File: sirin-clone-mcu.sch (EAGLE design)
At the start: 55 parts, among them J1 PJ-002A, J3 30_PIN_CONNECTOR_MALE, J5 SWITCHCRAFT_PHONEJACK, J6 SWD_CONNECTOR, T2 MCP1825S, U4 SGTL5000_32QFN, U5 23LC1024

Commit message: ready for gerbers
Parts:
- removed C4: 2.2UF, moon-germs-v1_main:2.2UF
- removed FUSE2: (no value), moon-germs-v1_main:FUSE
- removed U$2: USB-B, sirin-clone-library:USB-B
- added C2, C5: 1UF, sirin-clone-library:1UF
- added J2: (no value), sirin-clone-library:USB_MICRO-B_HALF_PTH_MILL
- L3: value FERRITE600 -> FER600
- R1: value 220OHM -> 220
- R2: value 470OHM -> 470
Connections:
- removed net N$27: J3.P$2
- removed net N$4: OK1.VO, R2.1
- removed net VUSB: FUSE2.2, U$2.VCC
- new net N$16: C5.-, U$3.6
- new net N$5: C5.+, U4.LINEOUTL(12)
- new net N$6: C2.+, U4.LINEOUTR(11)
- new net N$7: C2.-, U$3.5
- net AGND: now also J3.P$29, J3.P$30
- net D+: now also J2.D+; no longer U$2.D+
- net D-: now also J2.D-; no longer U$2.D-
- net GND: now also J2.GND, J2.SHIELD, J3.P$13, U$3.4; no longer C4.-, J3.P$29, J3.P$30, U$2.GND
- net PIN0/MIDIIN: now also OK1.VO, R2.1
- net PIN20/KNOB4: now also J3.P$3; no longer J3.P$4
- net PIN21/KNOB5: now also J3.P$4; no longer J3.P$5
- net PIN26/KNOB6: now also J3.P$8; no longer J3.P$9
- net PIN31/KNOB11: now also J3.P$7; no longer J3.P$8
- net PIN5/SW4: now also J3.P$5; no longer J3.P$6
- net PIN8/MIDILED: now also J3.P$2; no longer J3.P$3
- net PINA10/KNOB12: now also J3.P$10; no longer J3.P$11
- net PINA11/KNOB13: now also J3.P$9; no longer J3.P$10
- net PINA12/KNOB14: now also J3.P$11; no longer J3.P$12
- net PINA13/KNOB15: now also J3.P$12; no longer J3.P$13
- net PINA14/KNOB16: now also J3.P$6; no longer J3.P$7
- net USB_ID: now also J2.ID
- net VUSB_IN: now also J2.VBUS; no longer C4.+, FUSE2.1
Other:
- moved on the sheet: U$3

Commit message: adding bom attributes
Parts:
- J2: device sirin-clone-library:USB_MICRO-B_HALF_PTH_MILL -> sirin-clone-library:USB_MICRO-B
- L3: device moon-germs-v1_main:FERRITE600 -> moon-germs-v1_main:FERRITE600_AUDIO
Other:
- moved on the sheet: J2
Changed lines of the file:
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@@
 <part name="GND1" library="sirin-clone-library" library_urn="urn:adsk.eagle:library:9336050" deviceset="GND" device=""/>
 <part name="GND2" library="sirin-clone-library" library_urn="urn:adsk.eagle:library:9336050" deviceset="GND" device=""/>
-<part name="J3" library="sirin-clone-library" library_urn="urn:adsk.eagle:library:9336050" deviceset="30_PIN_CONNECTOR_MALE" device="" package3d_urn="urn:adsk.eagle:package:9975532/3"/>
+<part name="J3" library="sirin-clone-library" library_urn="urn:adsk.eagle:library:9336050" deviceset="30_PIN_CONNECTOR_MALE" device="" package3d_urn="urn:adsk.eagle:package:9975532/4"/>
 <part name="GND3" library="sirin-clone-library" library_urn="urn:adsk.eagle:library:9336050" deviceset="GND" device=""/>
 <part name="K3" library="moon-germs-v1_main" library_urn="urn:adsk.eagle:library:8442267" deviceset="MK20DX256VLH7" device="" package3d_urn="urn:adsk.eagle:package:8700970/2"/>
@@
 <part name="R5" library="moon-germs-v1_main" library_urn="urn:adsk.eagle:library:8442267" deviceset="33OHM" device="" package3d_urn="urn:adsk.eagle:package:8442354/2" value="33"/>
 <part name="R6" library="moon-germs-v1_main" library_urn="urn:adsk.eagle:library:8442267" deviceset="33OHM" device="" package3d_urn="urn:adsk.eagle:package:8442354/2" value="33"/>
-<part name="J6" library="moon-germs-v1_main" library_urn="urn:adsk.eagle:library:8442267" deviceset="SWD_CONNECTOR" device=""/>
+<part name="J6" library="moon-germs-v1_main" library_urn="urn:adsk.eagle:library:8442267" deviceset="SWD_CONNECTOR" device="" package3d_urn="urn:adsk.eagle:package:8709581/1"/>
 <part name="GND9" library="moon-germs-v1_main" library_urn="urn:adsk.eagle:library:8442267" deviceset="GND" device=""/>
 <part name="S2" library="moon-germs-v1_main" library_urn="urn:adsk.eagle:library:8442267" deviceset="TACT_SWITCH" device="" package3d_urn="urn:adsk.eagle:package:8762249/2"/>
@@
 <part name="C36" library="moon-germs-v1_main" library_urn="urn:adsk.eagle:library:8442267" deviceset="0.15UF" device="" package3d_urn="urn:adsk.eagle:package:8442351/2"/>
 <part name="D6" library="moon-germs-v1" deviceset="AP7313" device=""/>
-<part name="L3" library="moon-germs-v1_main" library_urn="urn:adsk.eagle:library:8442267" deviceset="FERRITE600" device="" package3d_urn="urn:adsk.eagle:package:8442354/2" value="FER600"/>
+<part name="L3" library="moon-germs-v1_main" library_urn="urn:adsk.eagle:library:8442267" deviceset="FERRITE600_AUDIO" device="" package3d_urn="urn:adsk.eagle:package:8442354/2" value="FER600"/>
 <part name="R11" library="moon-germs-v1_main" library_urn="urn:adsk.eagle:library:8442267" deviceset="2.2KOHM" device="" package3d_urn="urn:adsk.eagle:package:8442354/2" value="2.2K"/>
 <part name="R12" library="moon-germs-v1_main" library_urn="urn:adsk.eagle:library:8442267" deviceset="2.2KOHM" device="" package3d_urn="urn:adsk.eagle:package:8442354/2" value="2.2K"/>
@@
 <part name="C5" library="sirin-clone-library" library_urn="urn:adsk.eagle:library:9336050" deviceset="1UF" device="" package3d_urn="urn:adsk.eagle:package:8442351/2"/>
 <part name="GND20" library="sirin-clone-library" library_urn="urn:adsk.eagle:library:9336050" deviceset="GND" device=""/>
-<part name="J2" library="sirin-clone-library" library_urn="urn:adsk.eagle:library:9336050" deviceset="USB_MICRO-B" device="_HALF_PTH_MILL" package3d_urn="urn:adsk.eagle:package:8711132/2"/>
+<part name="J2" library="sirin-clone-library" library_urn="urn:adsk.eagle:library:9336050" deviceset="USB_MICRO-B" device="" package3d_urn="urn:adsk.eagle:package:10018607/2"/>
 <part name="GND8" library="moon-germs-v1_main" library_urn="urn:adsk.eagle:library:8442267" deviceset="GND" device=""/>
 </parts>

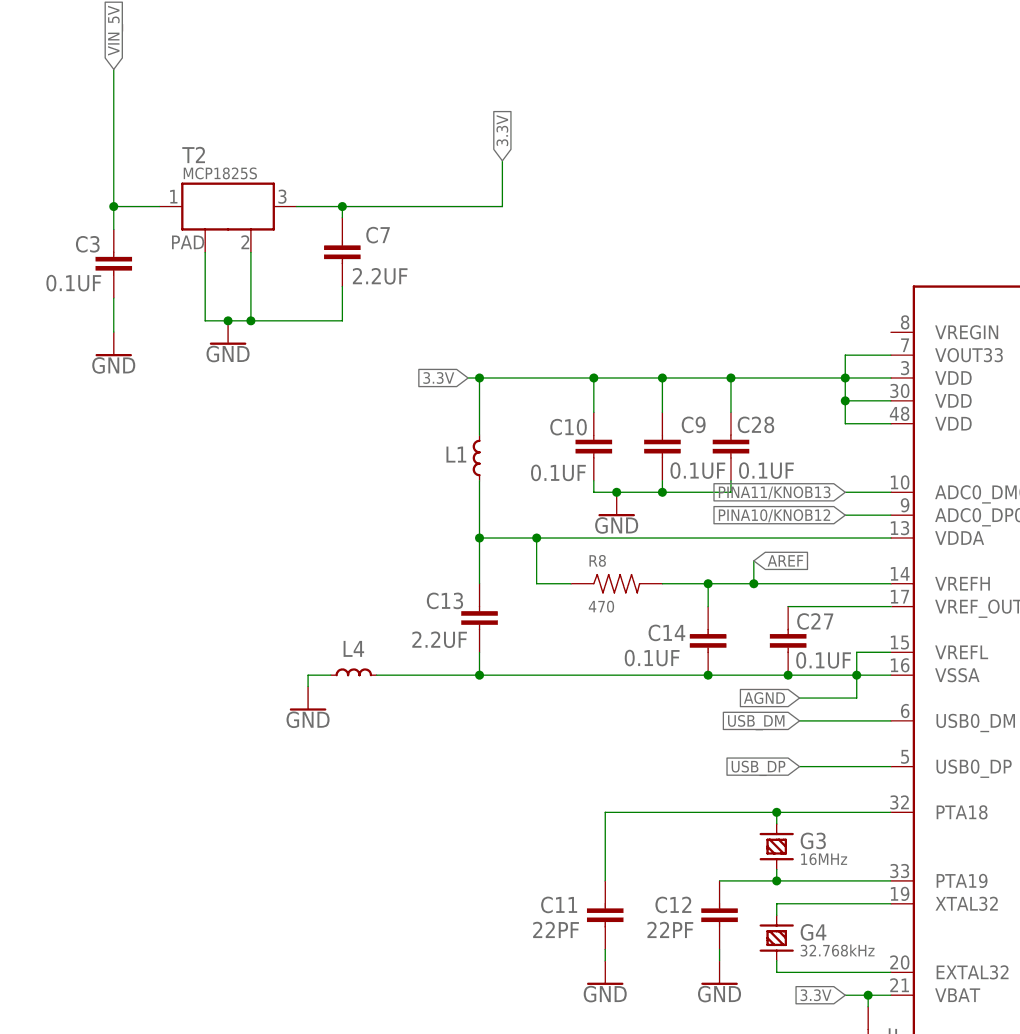
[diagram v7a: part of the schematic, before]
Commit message: placed bom order
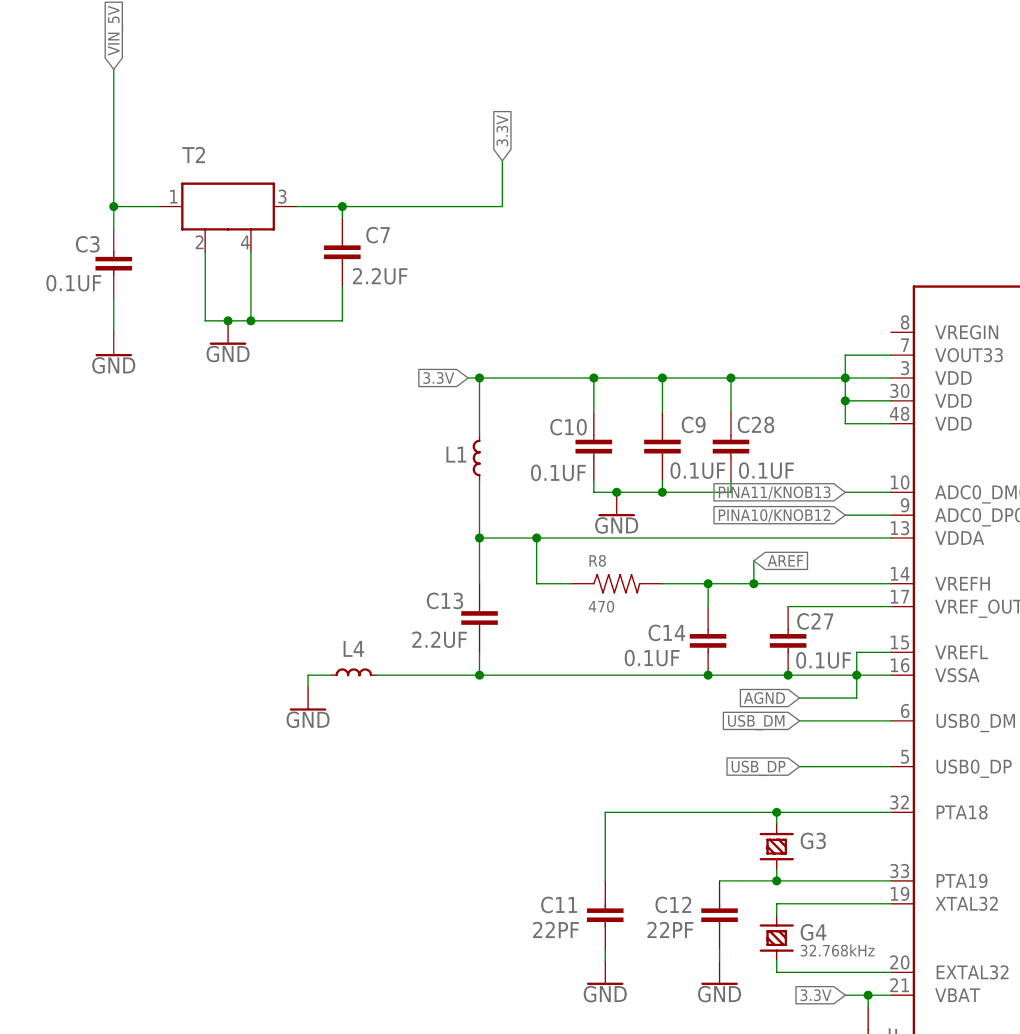
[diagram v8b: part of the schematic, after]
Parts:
- D6: device moon-germs-v1:AP7313 -> moon-germs-v1_main:AP7313
- J5: device moon-germs-v1_main:SWITCHCRAFT_PHONEJACK -> sirin-clone-library:SWITCHCRAFT_PHONEJACK
- T2: device moon-germs-v1_main:LDO -> sirin-clone-library:MCP1826SMSTT3
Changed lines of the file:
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@@
 <?xml version="1.0" encoding="utf-8"?>
 <!DOCTYPE eagle SYSTEM "eagle.dtd">
-<eagle version="9.3.1">
+<eagle version="9.3.2">
 <drawing>
 <settings>
@@
 <part name="K3" library="moon-germs-v1_main" library_urn="urn:adsk.eagle:library:8442267" deviceset="MK20DX256VLH7" device="" package3d_urn="urn:adsk.eagle:package:8700970/2"/>
 <part name="K4" library="moon-germs-v1_main" library_urn="urn:adsk.eagle:library:8442267" deviceset="MKL04Z32VLC4" device="" package3d_urn="urn:adsk.eagle:package:8700971/2"/>
-<part name="T2" library="moon-germs-v1_main" library_urn="urn:adsk.eagle:library:8442267" deviceset="LDO" device="" package3d_urn="urn:adsk.eagle:package:8700968/2" value="MCP1825S"/>
+<part name="T2" library="sirin-clone-library" library_urn="urn:adsk.eagle:library:9336050" deviceset="MCP1826S" device="MSTT3" package3d_urn="urn:adsk.eagle:package:30370/1" value="MCP1825S"/>
 <part name="G3" library="moon-germs-v1_main" library_urn="urn:adsk.eagle:library:8442267" deviceset="CRYSTAL-" device="HC49US" package3d_urn="urn:adsk.eagle:package:8700963/2" value="16MHz"/>
 <part name="G4" library="moon-germs-v1_main" library_urn="urn:adsk.eagle:library:8442267" deviceset="CRYSTAL-" device="TC26H" package3d_urn="urn:adsk.eagle:package:8700964/2" value="32.768kHz"/>
@@
 <part name="C35" library="moon-germs-v1_main" library_urn="urn:adsk.eagle:library:8442267" deviceset="0.1UF" device="" package3d_urn="urn:adsk.eagle:package:8442351/2"/>
 <part name="C36" library="moon-germs-v1_main" library_urn="urn:adsk.eagle:library:8442267" deviceset="0.15UF" device="" package3d_urn="urn:adsk.eagle:package:8442351/2"/>
-<part name="D6" library="moon-germs-v1" deviceset="AP7313" device=""/>
+<part name="D6" library="moon-germs-v1_main" library_urn="urn:adsk.eagle:library:8442267" deviceset="AP7313" device="" package3d_urn="urn:adsk.eagle:package:8442353/2"/>
 <part name="L3" library="moon-germs-v1_main" library_urn="urn:adsk.eagle:library:8442267" deviceset="FERRITE600_AUDIO" device="" package3d_urn="urn:adsk.eagle:package:8442354/2" value="FER600"/>
 <part name="R11" library="moon-germs-v1_main" library_urn="urn:adsk.eagle:library:8442267" deviceset="2.2KOHM" device="" package3d_urn="urn:adsk.eagle:package:8442354/2" value="2.2K"/>
@@
 <part name="R14" library="moon-germs-v1_main" library_urn="urn:adsk.eagle:library:8442267" deviceset="10KOHM" device="" package3d_urn="urn:adsk.eagle:package:8442354/2" value="10K"/>
 <part name="GND43" library="moon-germs-v1" deviceset="GND" device=""/>
-<part name="J5" library="moon-germs-v1_main" library_urn="urn:adsk.eagle:library:8442267" deviceset="SWITCHCRAFT_PHONEJACK" device="" package3d_urn="urn:adsk.eagle:package:8442329/2"/>
+<part name="J5" library="sirin-clone-library" library_urn="urn:adsk.eagle:library:9336050" deviceset="SWITCHCRAFT_PHONEJACK" device="" package3d_urn="urn:adsk.eagle:package:8442329/2"/>
 <part name="C2" library="sirin-clone-library" library_urn="urn:adsk.eagle:library:9336050" deviceset="1UF" device="" package3d_urn="urn:adsk.eagle:package:8442351/2"/>
 <part name="C5" library="sirin-clone-library" library_urn="urn:adsk.eagle:library:9336050" deviceset="1UF" device="" package3d_urn="urn:adsk.eagle:package:8442351/2"/>
@@
 <instance part="T2" gate="G$1" x="-261.62" y="234.95" smashed="yes">
 <attribute name="NAME" x="-266.7" y="239.776" size="1.778" layer="95"/>
-<attribute name="VALUE" x="-266.7" y="237.998" size="1.27" layer="96"/>
 </instance>
 <instance part="G3" gate="G$1" x="-200.66" y="163.83" smashed="yes" rot="R270">
 <attribute name="NAME" x="-198.12" y="163.576" size="1.778" layer="95" ratio="10"/>
-<attribute name="VALUE" x="-198.12" y="161.798" size="1.27" layer="96" ratio="10"/>
 </instance>
 <instance part="G4" gate="G$1" x="-200.66" y="153.67" smashed="yes" rot="R270">
